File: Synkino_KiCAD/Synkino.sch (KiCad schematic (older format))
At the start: 12 parts

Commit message: wip Schematics
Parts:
- added C? (x4): 1µ, symbol C
- added C?: 100n, symbol C_Small
- added C? (x2): 33p, symbol C_Small
- added R? (x2): 100k, symbol R
- added R?: 1M, symbol R
- added U?: AP7312-1833W6-7, symbol AP7312-1833W6-7
- added U?: VS1053B, symbol VS1053B
- added Y?: Crystal, symbol Crystal
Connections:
- net GNDD: now also C?.2, C?.2, C?.2, C?.2, C?.2, C?.2, R?.2, U?.16 (DGND1), U?.2 (GND), U?.20 (DGND2), U?.21 (DGND3), U?.22 (DGND4), U?.35 (GND), U?.4 (DGND0)
- new net: C?.1, R?.2, U?.17 (XTALO), Y?.2
- new net: C?.1, R?.1, U?.18 (XTALI), Y?.1
- new net: C?.1, R?.2, U?.3 (~XRESET)
- new net: C?.1, U?.44 (RCAP)
- new net +1V8: C?.1, U?.24 (CVDD2), U?.31 (CVDD3), U?.5 (CVDD0), U?.6 (VOUT1), U?.7 (CVDD1)
- new net +3V3: C?.1, U?.1 (VOUT2), U?.14 (IOVDD1), U?.19 (IOVDD2), U?.6 (IOVDD0)
- new net DREQ: U?.8 (DREQ)
- new net GNDA: C?.2, U?.37 (AGND0), U?.40 (AGND1), U?.41 (AGND2), U?.47 (AGND3)
- new net GPIO_PLLDWN: R?.1, U?.10 (GPIO3/SDATA), U?.11 (GPIO6/I2S_SCLK), U?.12 (GPIO7/I2S_SDATA), U?.25 (GPIO5_/_I2S_MCLK), U?.33 (GPIO0), U?.34 (GPIO1), U?.36 (GPIO4/I2S_LROUT), U?.9 (GPIO2/DCLK)
- new net VDC: C?.1, U?.3 (EN2), U?.4 (EN1), U?.5 (VIN)
- new net VDDA: R?.1
- new net XDCS: U?.13 (XDCS/BSYNC)
- no-connect marks 0 -> 4

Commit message: Adding files
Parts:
- added R?: 100k, symbol R
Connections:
- net +3V3: now also U?.32 (~XTEST), R?.1
- net VDDA: now also U?.38 (AVDD0), U?.43 (AVDD1), U?.45 (AVDD2)
- net CS_3V: now reaches U?.23 (~XCS)
- net at U?.26 (RX): now also R?.2
- net SCLK_3V: now reaches U?.28 (SCLK)
- net MOSI_3V: now reaches U?.29 (SI)
- net RST_3V: now reaches C?.1, R?.2, U?.3 (~XRESET)
- net MISO_3V: now reaches U?.30 (SO)
- net ROUT: now reaches U?.39 (RIGHT)
- net LOUT: now reaches U?.46 (LEFT)
- net XDCS renamed XDCS_3V
- no-connect marks 4 -> 5
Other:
- moved on the sheet: C?, R?

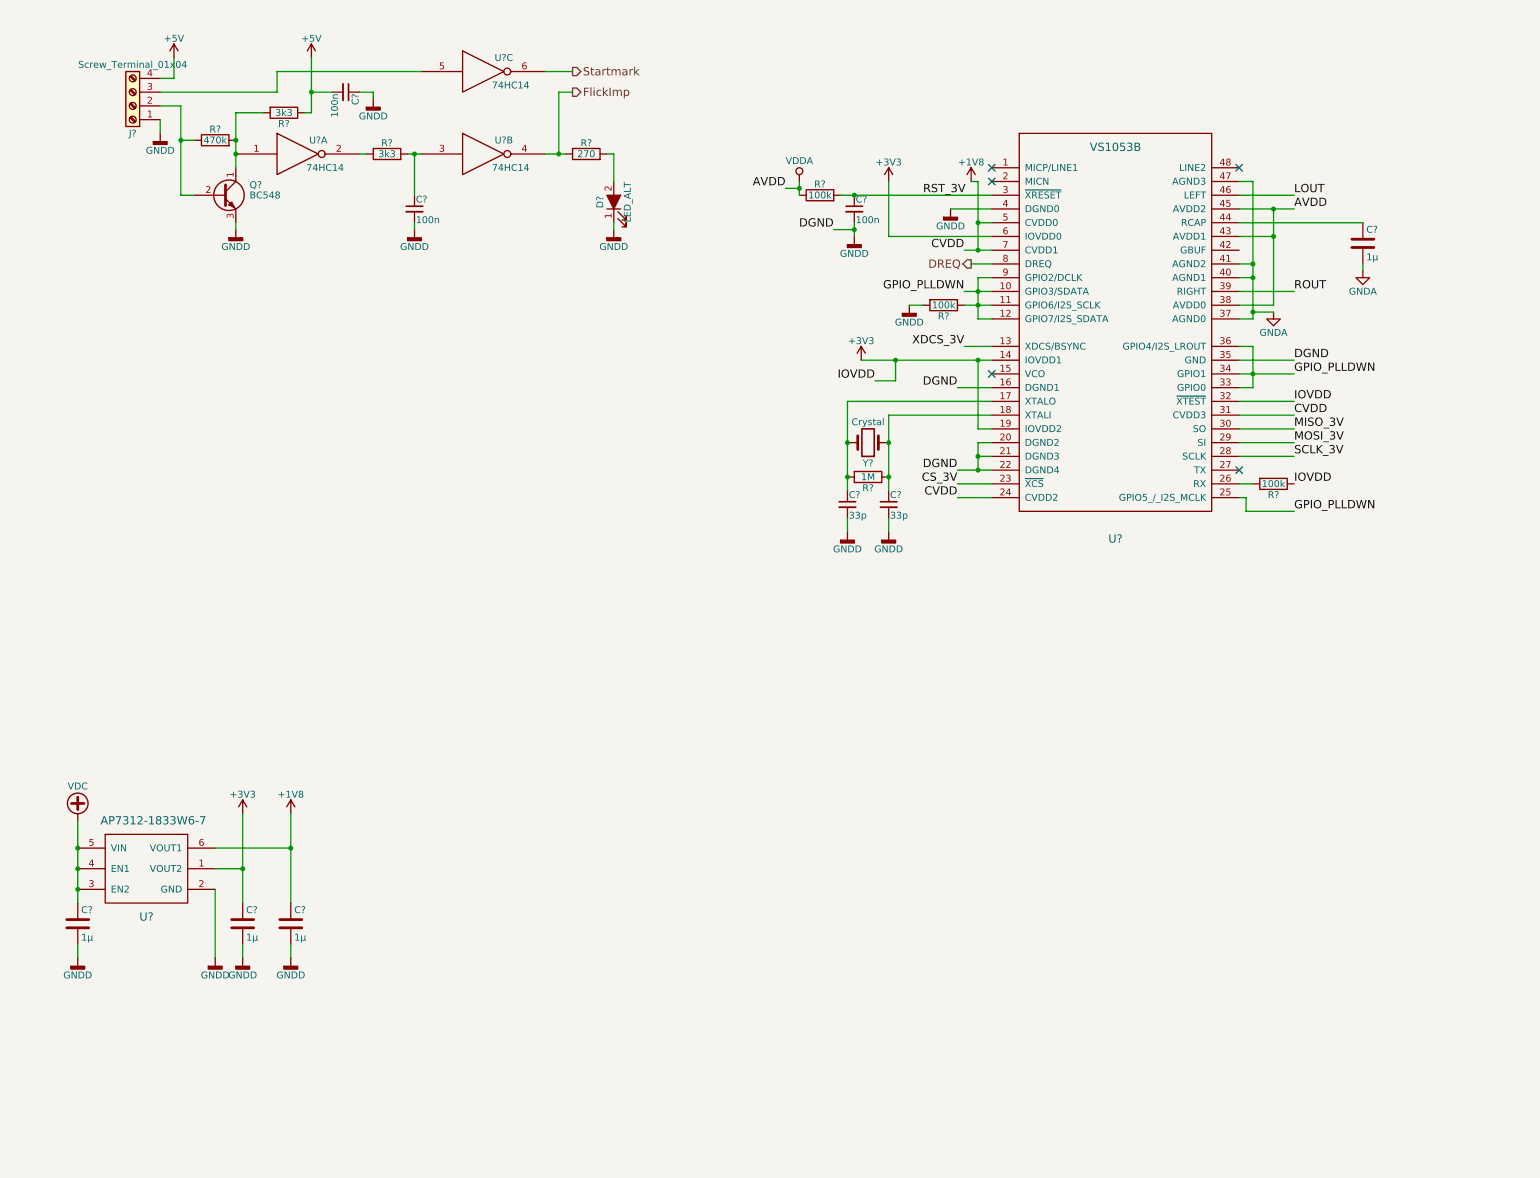
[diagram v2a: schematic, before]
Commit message: Adding Sigma-Delta Reconstruction Filter
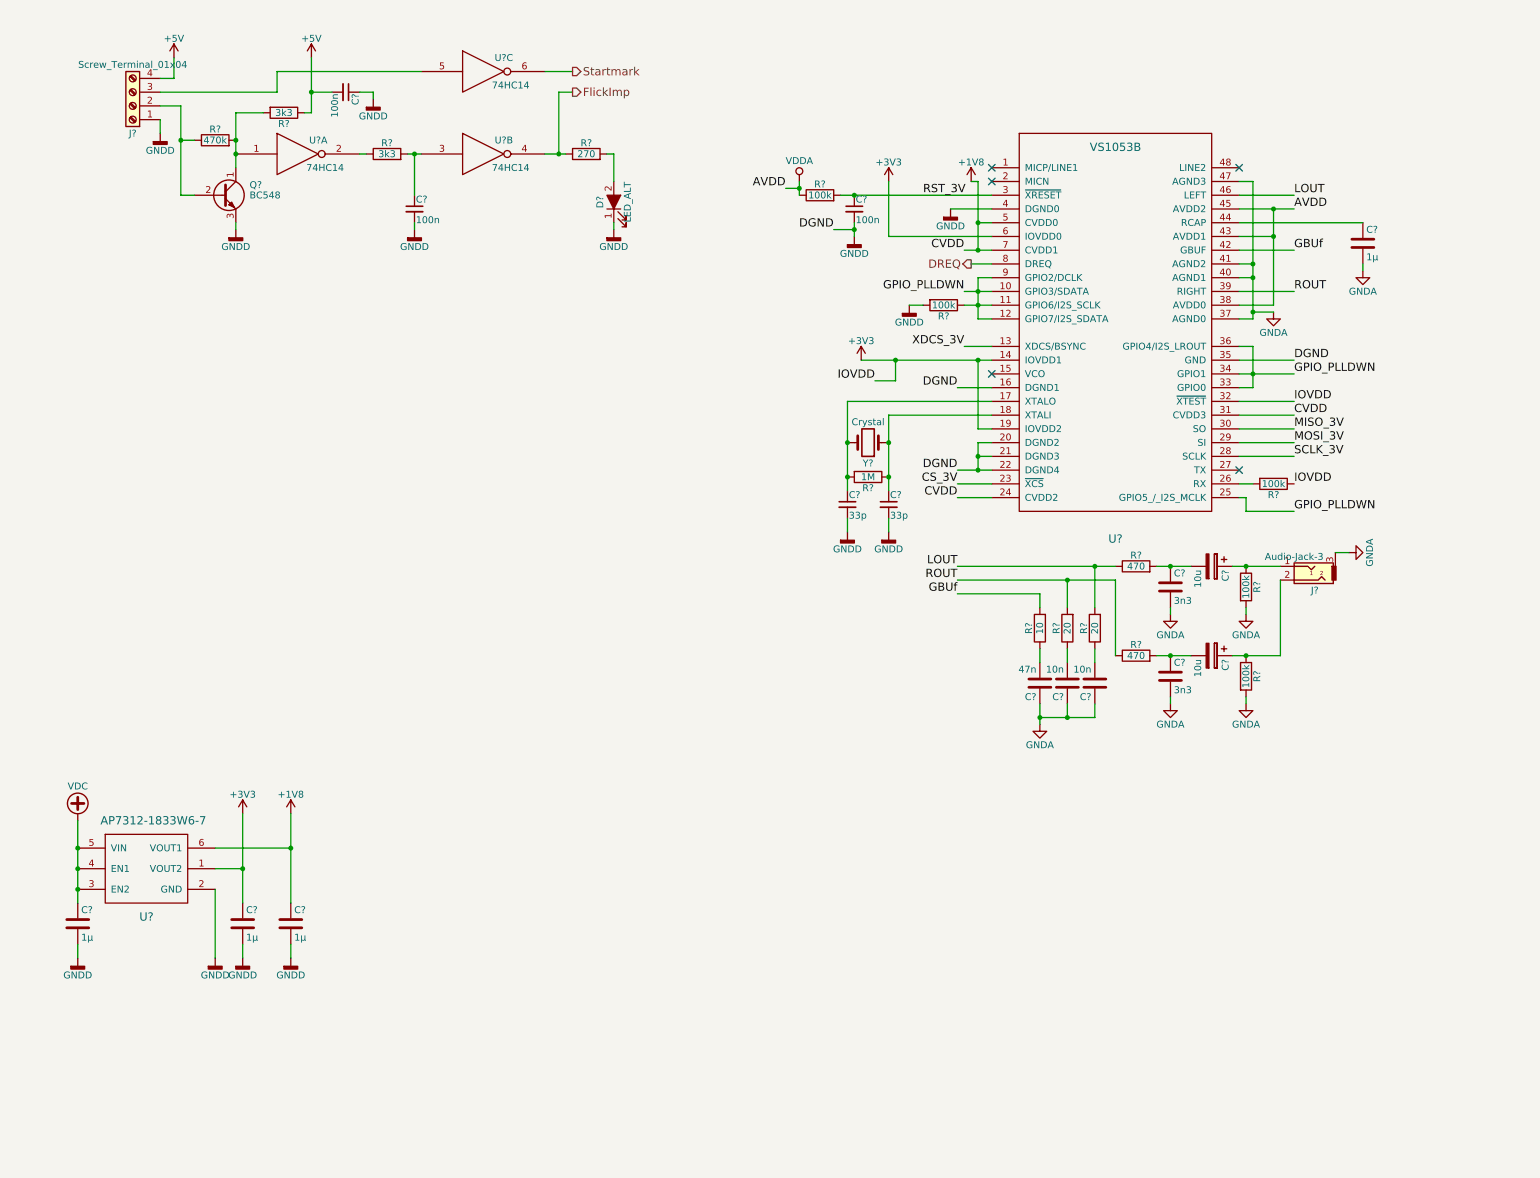
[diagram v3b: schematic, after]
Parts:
- added C? (x2): 10n, symbol C
- added C?: 47n, symbol C
- added C? (x2): 3n3, symbol C
- added C? (x2): 10u, symbol CP
- added J?: Audio-Jack-3, symbol Audio-Jack-3
- added R? (x2): 20, symbol R
- added R?: 10, symbol R
- added R? (x2): 470, symbol R
- added R? (x2): 100k, symbol R
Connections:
- net GNDA: now also C?.1, C?.1, C?.1, C?.2, C?.2, J?.3, R?.2, R?.2
- net LOUT: now also R?.1, R?.2
- net ROUT: now also R?.1, R?.2
- net GBUf: now reaches U?.42 (GBUF)
- net GBUf: now also R?.2
- new net: C?.2, R?.1 (x3)
- new net: C?.1, J?.1, R?.1
- new net: C?.1, J?.2, R?.1
- new net: C?.1, C?.2, R?.2 (x2)

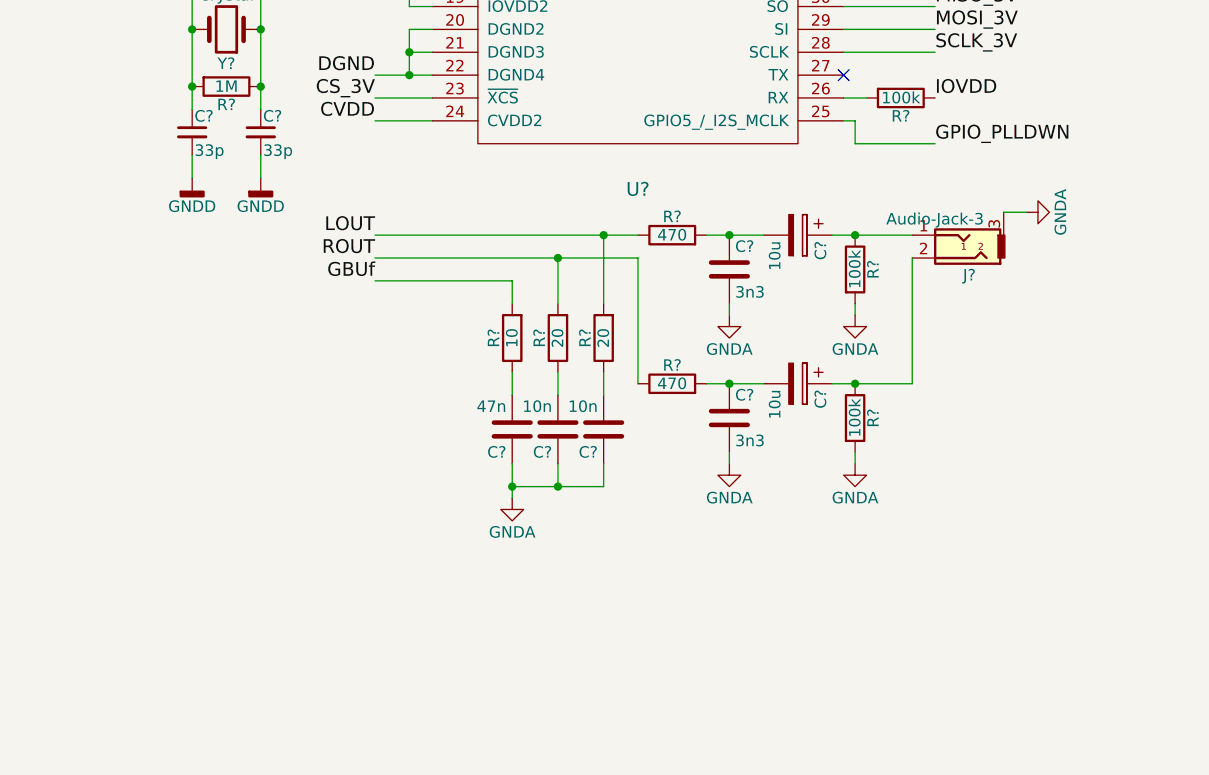
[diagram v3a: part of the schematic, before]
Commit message: Adding de-click analog switch for delayed audio power-on
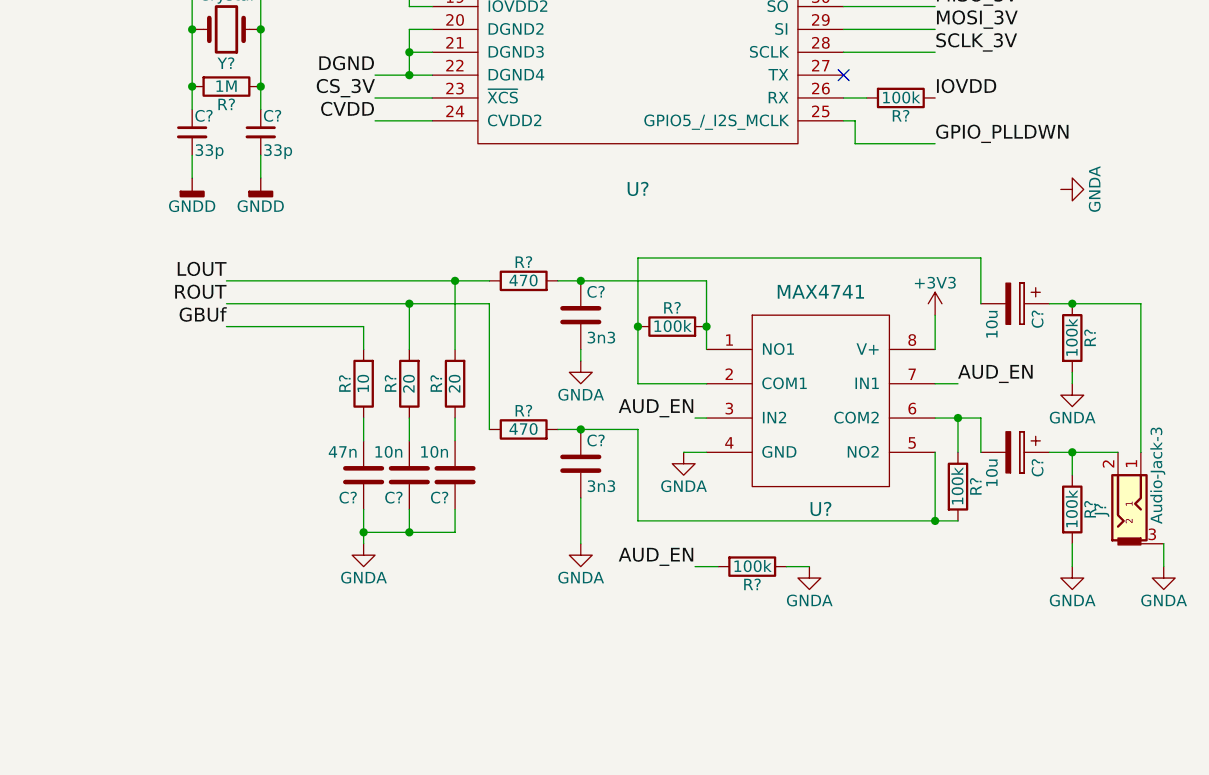
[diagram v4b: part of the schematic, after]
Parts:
- added R? (x3): 100k, symbol R
- added U?: MAX4741, symbol MAX4741
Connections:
- net +3V3: now also U?.8 (V+)
- net GNDA: now also R?.1, U?.4 (GND)
- net at C?.1, R?.2: now also R?.2, U?.1 (NO1); no longer C?.2
- net at C?.1, R?.2: now also R?.2, U?.5 (NO2); no longer C?.2
- new net: C?.2, R?.1, U?.2 (COM1)
- new net: C?.2, R?.1, U?.6 (COM2)
- new net AUD_EN: R?.2, U?.3 (IN2), U?.7 (IN1)
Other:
- moved on the sheet: C?, J?, R?
